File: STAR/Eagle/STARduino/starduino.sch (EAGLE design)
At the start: 52 parts, among them J1 J30J-25, U1 PCA9515A, U10 PCA9306DCT, U11 CC2, U12 SSCMNNN015PA2A3, U2 ATSAMD21G18, U3 MAX31725MTA+, U4 MC74VHC1GT125, U5 DS3231MZ+, U6 MC14504BDTG, U7 BMX055, U8 ADXL375BCCZ, U9 TCA9535_RTW_24

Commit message: Power Board
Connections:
- removed net EN_28V: U2.PA28/EIC
- removed net I_SENSE: U2.PA05/EIC/AIN5/SCOM0PAD1
- removed net LED_CTRL: U2.PA09/I2C/EIC/AIN17/SCOM2PAD1+/TC0
- removed net PB22: U2.PB22/EIC/SCOM5PAD2
- removed net PB23: U2.PB23/EIC/SCOM5PAD3
- removed net PI_KILL: U2.PA16/I2C/EIC/SCOM1PAD0+/TC2
- removed net RX0: U2.PA11/EIC/AIN19/SCOM2PAD3+/TC1
- removed net RX1: U2.PA19/EIC/SCOM1PAD3+/TC3
- removed net RX2: U2.PA21/EIC/SCOM5PAD3+
- removed net STEPFREQ: U2.PA08/I2C/AIN16/SCOM2PAD0+/TC0
- removed net SYNC: U2.PA15/XOUT/EIC/SCOM2PAD3+/TC3
- removed net TX0: U2.PA10/EIC/AIN18/SCOM2PAD2+/TC1
- removed net TX1: U2.PA18/EIC/SCOM1PAD2+/TC3
- removed net TX2: U2.PA20/EIC/SCOM5PAD2+
- removed net USB_D_N: U2.PA24/EIC/SCOM3PAD2+/TC5
- removed net USB_D_P: U2.PA25/EIC/SCOM3PAD3+/TC5
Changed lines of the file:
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@@
-</segment>
-</net>
-<net name="I_SENSE" class="2">
-<segment>
-<pinref part="U2" gate="G$1" pin="PA05/EIC/AIN5/SCOM0PAD1"/>
-<wire x1="314.96" y1="391.16" x2="347.98" y2="391.16" width="0.1524" layer="91"/>
-<label x="347.98" y="391.16" size="1.016" layer="95" xref="yes"/>
 </segment>
 </net>
@@
 </segment>
 </net>
-<net name="TX1" class="0">
-<segment>
-<pinref part="U2" gate="G$1" pin="PA18/EIC/SCOM1PAD2+/TC3"/>
-<wire x1="314.96" y1="358.14" x2="347.98" y2="358.14" width="0.1524" layer="91"/>
-<label x="347.98" y="358.14" size="1.016" layer="95" xref="yes"/>
-</segment>
-</net>
-<net name="RX1" class="0">
-<segment>
-<pinref part="U2" gate="G$1" pin="PA19/EIC/SCOM1PAD3+/TC3"/>
-<wire x1="314.96" y1="355.6" x2="347.98" y2="355.6" width="0.1524" layer="91"/>
-<label x="347.98" y="355.6" size="1.016" layer="95" xref="yes"/>
-</segment>
-</net>
 <net name="NFAULT" class="0">
 <segment>
@@
 <wire x1="228.6" y1="185.42" x2="226.06" y2="185.42" width="0.1524" layer="91"/>
 <label x="228.6" y="185.42" size="1.016" layer="95" xref="yes"/>
-</segment>
-</net>
-<net name="PB22" class="0">
-<segment>
-<pinref part="U2" gate="G$1" pin="PB22/EIC/SCOM5PAD2"/>
-<wire x1="314.96" y1="317.5" x2="347.98" y2="317.5" width="0.1524" layer="91"/>
-<label x="347.98" y="317.5" size="1.016" layer="95" xref="yes"/>
-</segment>
-</net>
-<net name="PB23" class="0">
-<segment>
-<pinref part="U2" gate="G$1" pin="PB23/EIC/SCOM5PAD3"/>
-<wire x1="314.96" y1="314.96" x2="347.98" y2="314.96" width="0.1524" layer="91"/>
-<label x="347.98" y="314.96" size="1.016" layer="95" xref="yes"/>
 </segment>
 </net>
@@
 </segment>
 </net>
-<net name="TX0" class="0">
-<segment>
-<pinref part="U2" gate="G$1" pin="PA10/EIC/AIN18/SCOM2PAD2+/TC1"/>
-<wire x1="314.96" y1="378.46" x2="347.98" y2="378.46" width="0.1524" layer="91"/>
-<label x="347.98" y="378.46" size="1.016" layer="95" xref="yes"/>
-</segment>
-</net>
-<net name="RX0" class="0">
-<segment>
-<pinref part="U2" gate="G$1" pin="PA11/EIC/AIN19/SCOM2PAD3+/TC1"/>
-<wire x1="314.96" y1="375.92" x2="347.98" y2="375.92" width="0.1524" layer="91"/>
-<label x="347.98" y="375.92" size="1.016" layer="95" xref="yes"/>
-</segment>
-</net>
 <net name="NSLEEP" class="0">
 <segment>
@@
 <wire x1="477.52" y1="236.22" x2="482.6" y2="236.22" width="0.1524" layer="91"/>
 <label x="482.6" y="236.22" size="1.016" layer="95" xref="yes"/>
-</segment>
-</net>
-<net name="STEPFREQ" class="0">
-<segment>
-<pinref part="U2" gate="G$1" pin="PA08/I2C/AIN16/SCOM2PAD0+/TC0"/>
-<wire x1="314.96" y1="383.54" x2="347.98" y2="383.54" width="0.1524" layer="91"/>
-<label x="347.98" y="383.54" size="1.016" layer="95" xref="yes"/>
 </segment>
 </net>
@@
 </segment>
 </net>
-<net name="TX2" class="0">
-<segment>
-<pinref part="U2" gate="G$1" pin="PA20/EIC/SCOM5PAD2+"/>
-<wire x1="314.96" y1="353.06" x2="347.98" y2="353.06" width="0.1524" layer="91"/>
-<label x="347.98" y="353.06" size="1.016" layer="95" xref="yes"/>
-</segment>
-</net>
-<net name="RX2" class="0">
-<segment>
-<pinref part="U2" gate="G$1" pin="PA21/EIC/SCOM5PAD3+"/>
-<wire x1="314.96" y1="350.52" x2="347.98" y2="350.52" width="0.1524" layer="91"/>
-<label x="347.98" y="350.52" size="1.016" layer="95" xref="yes"/>
-</segment>
-</net>
 <net name="DEC0" class="0">
 <segment>
@@
 </segment>
 </net>
-<net name="LED_CTRL" class="0">
-<segment>
-<pinref part="U2" gate="G$1" pin="PA09/I2C/EIC/AIN17/SCOM2PAD1+/TC0"/>
-<wire x1="314.96" y1="381" x2="347.98" y2="381" width="0.1524" layer="91"/>
-<label x="347.98" y="381" size="1.016" layer="95" xref="yes"/>
-</segment>
-</net>
-<net name="SYNC" class="0">
-<segment>
-<pinref part="U2" gate="G$1" pin="PA15/XOUT/EIC/SCOM2PAD3+/TC3"/>
-<wire x1="314.96" y1="365.76" x2="347.98" y2="365.76" width="0.1524" layer="91"/>
-<label x="347.98" y="365.76" size="1.016" layer="95" xref="yes"/>
-</segment>
-</net>
-<net name="PI_KILL" class="0">
-<segment>
-<pinref part="U2" gate="G$1" pin="PA16/I2C/EIC/SCOM1PAD0+/TC2"/>
-<wire x1="314.96" y1="363.22" x2="347.98" y2="363.22" width="0.1524" layer="91"/>
-<label x="347.98" y="363.22" size="1.016" layer="95" xref="yes"/>
-</segment>
-</net>
 <net name="SCL_BUFF" class="0">
 <segment>
@@
 <label x="510.54" y="340.36" size="1.016" layer="95" xref="yes"/>
 <pinref part="R7" gate="A" pin="1"/>
-</segment>
-</net>
-<net name="EN_28V" class="0">
-<segment>
-<pinref part="U2" gate="G$1" pin="PA28/EIC"/>
-<wire x1="314.96" y1="335.28" x2="347.98" y2="335.28" width="0.1524" layer="91"/>
-<label x="347.98" y="335.28" size="1.016" layer="95" xref="yes"/>
 </segment>
 </net>
@@
 </segment>
 </net>
-<net name="USB_D_P" class="0">
-<segment>
-<pinref part="U2" gate="G$1" pin="PA25/EIC/SCOM3PAD3+/TC5"/>
-<wire x1="314.96" y1="340.36" x2="347.98" y2="340.36" width="0.1524" layer="91"/>
-<label x="347.98" y="340.36" size="1.016" layer="95" xref="yes"/>
-</segment>
-</net>
-<net name="USB_D_N" class="0">
-<segment>
-<pinref part="U2" gate="G$1" pin="PA24/EIC/SCOM3PAD2+/TC5"/>
-<wire x1="314.96" y1="342.9" x2="347.98" y2="342.9" width="0.1524" layer="91"/>
-<label x="347.98" y="342.9" size="1.016" layer="95" xref="yes"/>
-</segment>
-</net>

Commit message: fixed choke routing on power board
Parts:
- added JP3: (no value), pinhead:PINHD-2X3
- added U$1: FODM8061-D, optoisolater:FODM8061-D
- J1: value J30J-25 -> J30J-9J30J; device CM_J30J:J30J-25 -> CM_J30J:J30J-9J30J
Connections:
- removed net DEC0: U9.P15
- removed net DEC1: U9.P13
- removed net DIR: U9.P12
- removed net I0: U9.P17
- removed net I1: U9.P16
- removed net M0: U9.P11
- removed net M1: U9.P10
- removed net NENBL: U9.P07
- removed net NFAULT: U9.P06
- removed net NSLEEP: U9.P14
- removed net SD_STAR: J1.9
- removed net VDD: J1.25
- new net MOTOR: U$1.AN, U2.PA05/EIC/AIN5/SCOM0PAD1
- new net MOTOR_GND: JP3.5, U$1.GND
- new net MOTOR_SIGNAL: JP3.3, U$1.VO
- new net MOTOR_VCC: JP3.1, U$1.VCC
- net +3V3: now also J1.6, J1.8, JP3.2; no longer J1.3
- net BIAS_REF: now also JP3.6; no longer J1.2
- net GND: now also J1.5, JP3.4, U$1.CAT; no longer J1.21, J1.22, J1.23, J1.24
- net MISO: now also J1.2; no longer J1.15
- net MOSI: now also J1.1; no longer J1.14
- net SCK: now also J1.3; no longer J1.16
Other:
- note added: "MOTOR DRIVER ISOLATER"

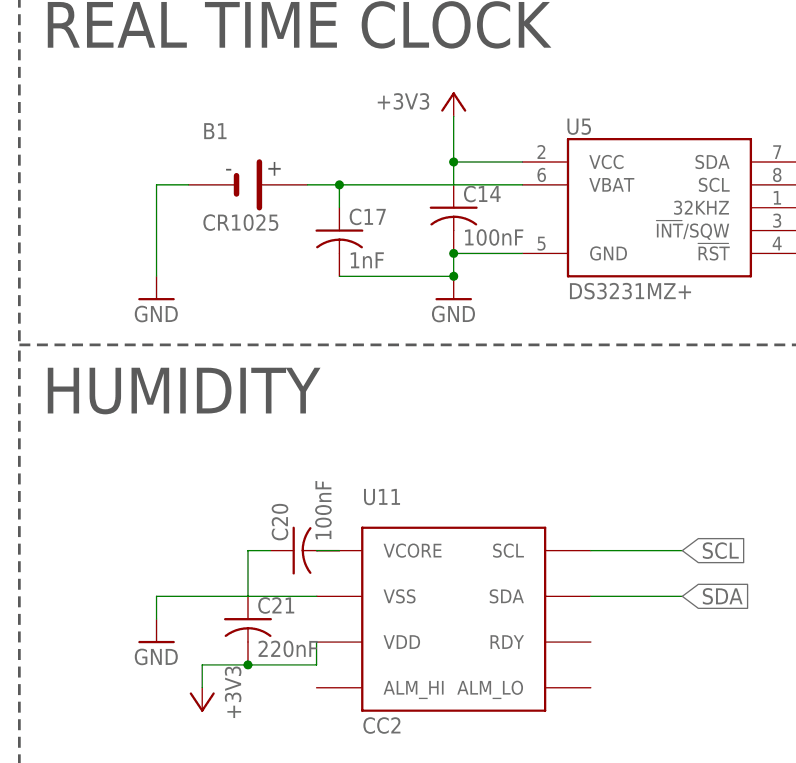
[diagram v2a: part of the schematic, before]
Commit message: Fixed all the wire stubs on Starduino
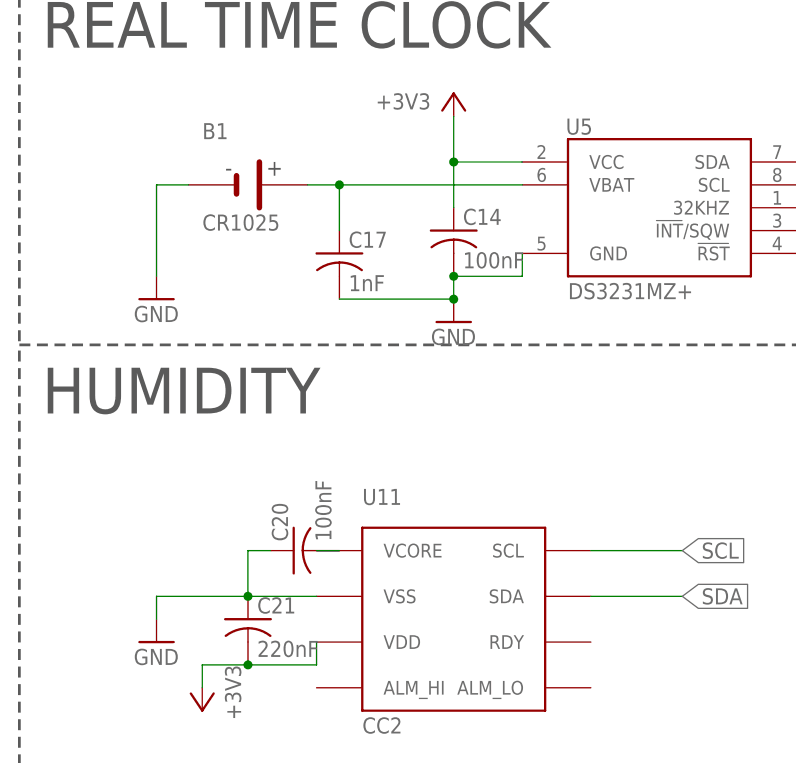
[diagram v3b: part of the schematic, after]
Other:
- moved on the sheet: C14, C17
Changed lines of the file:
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@@
 <?xml version="1.0" encoding="utf-8"?>
 <!DOCTYPE eagle SYSTEM "eagle.dtd">
-<eagle version="7.6.0">
+<eagle version="9.1.0">
 <drawing>
 <settings>
 <setting alwaysvectorfont="no"/>
+<setting keepoldvectorfont="yes"/>
 <setting verticaltext="up"/>
 </settings>
@@
 <instance part="U5" gate="G$1" x="78.74" y="266.7"/>
 <instance part="B1" gate="G$1" x="33.02" y="269.24"/>
-<instance part="C14" gate="G$1" x="55.88" y="266.7"/>
+<instance part="C14" gate="G$1" x="55.88" y="264.16"/>
 <instance part="+3V314" gate="G$1" x="55.88" y="279.4" smashed="yes">
 <attribute name="VALUE" x="53.34" y="279.4" size="1.778" layer="96" rot="R180"/>
 </instance>
-<instance part="GND19" gate="1" x="55.88" y="256.54"/>
+<instance part="GND19" gate="1" x="55.88" y="254"/>
 <instance part="GND18" gate="1" x="22.86" y="256.54"/>
-<instance part="C17" gate="G$1" x="43.18" y="264.16"/>
+<instance part="C17" gate="G$1" x="43.18" y="261.62"/>
 <instance part="U7" gate="G$1" x="213.36" y="254"/>
 <instance part="+3V312" gate="G$1" x="160.02" y="281.94" smashed="yes">
@@
 <wire x1="55.88" y1="276.86" x2="55.88" y2="271.78" width="0.1524" layer="91"/>
 <pinref part="U5" gate="G$1" pin="VCC"/>
-<wire x1="55.88" y1="271.78" x2="55.88" y2="269.24" width="0.1524" layer="91"/>
+<wire x1="55.88" y1="271.78" x2="55.88" y2="266.7" width="0.1524" layer="91"/>
 <wire x1="55.88" y1="271.78" x2="63.5" y2="271.78" width="0.1524" layer="91"/>
 <junction x="55.88" y="271.78"/>
@@
 </segment>
 <segment>
+<pinref part="C14" gate="G$1" pin="2"/>
+<pinref part="GND19" gate="1" pin="GND"/>
+<wire x1="55.88" y1="259.08" x2="55.88" y2="256.54" width="0.1524" layer="91"/>
+<pinref part="C17" gate="G$1" pin="2"/>
+<wire x1="43.18" y1="256.54" x2="55.88" y2="256.54" width="0.1524" layer="91"/>
+<junction x="55.88" y="256.54"/>
 <pinref part="U5" gate="G$1" pin="GND"/>
-<pinref part="C14" gate="G$1" pin="2"/>
-<wire x1="63.5" y1="261.62" x2="55.88" y2="261.62" width="0.1524" layer="91"/>
-<pinref part="GND19" gate="1" pin="GND"/>
-<wire x1="55.88" y1="261.62" x2="55.88" y2="259.08" width="0.1524" layer="91"/>
-<junction x="55.88" y="261.62"/>
-<pinref part="C17" gate="G$1" pin="2"/>
-<wire x1="43.18" y1="259.08" x2="55.88" y2="259.08" width="0.1524" layer="91"/>
+<wire x1="55.88" y1="259.08" x2="63.5" y2="259.08" width="0.1524" layer="91"/>
+<wire x1="63.5" y1="259.08" x2="63.5" y2="261.62" width="0.1524" layer="91"/>
 <junction x="55.88" y="259.08"/>
 </segment>
@@
 <wire x1="33.02" y1="228.6" x2="33.02" y2="223.52" width="0.1524" layer="91"/>
 <pinref part="C21" gate="G$1" pin="1"/>
+<junction x="33.02" y="223.52"/>
 </segment>
 <segment>
@@
 <pinref part="C17" gate="G$1" pin="1"/>
 <pinref part="U5" gate="G$1" pin="VBAT"/>
-<wire x1="43.18" y1="266.7" x2="43.18" y2="269.24" width="0.1524" layer="91"/>
+<wire x1="43.18" y1="264.16" x2="43.18" y2="269.24" width="0.1524" layer="91"/>
 <wire x1="43.18" y1="269.24" x2="63.5" y2="269.24" width="0.1524" layer="91"/>
 <pinref part="B1" gate="G$1" pin="+"/>
